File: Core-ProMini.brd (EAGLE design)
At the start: 99.8 x 68.8 mm, 27 parts, among them CON1 5.08, CON2 2mm, CON3 0.100, IC1 cj7805, J2 IO4, J4 2.1mm, J5 IO4, J6 IO4, J7 IO4

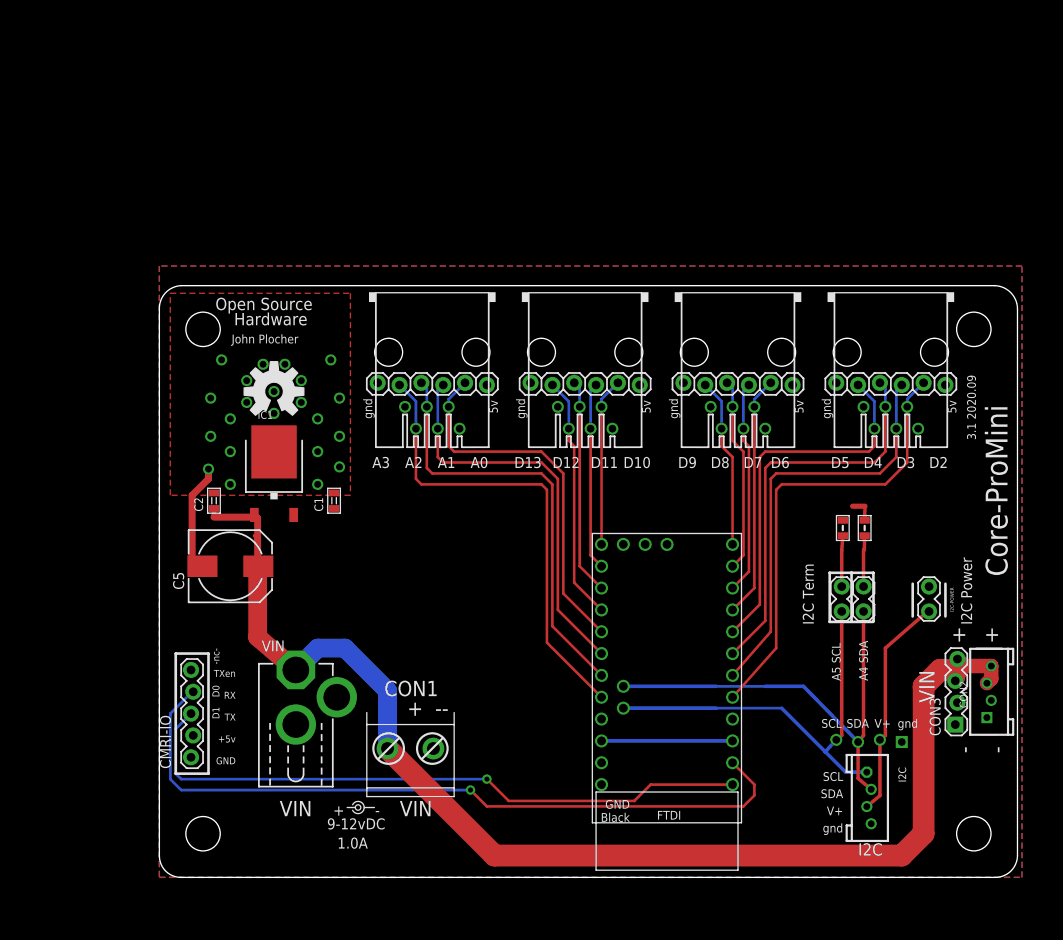
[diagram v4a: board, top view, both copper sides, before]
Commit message: normalized values
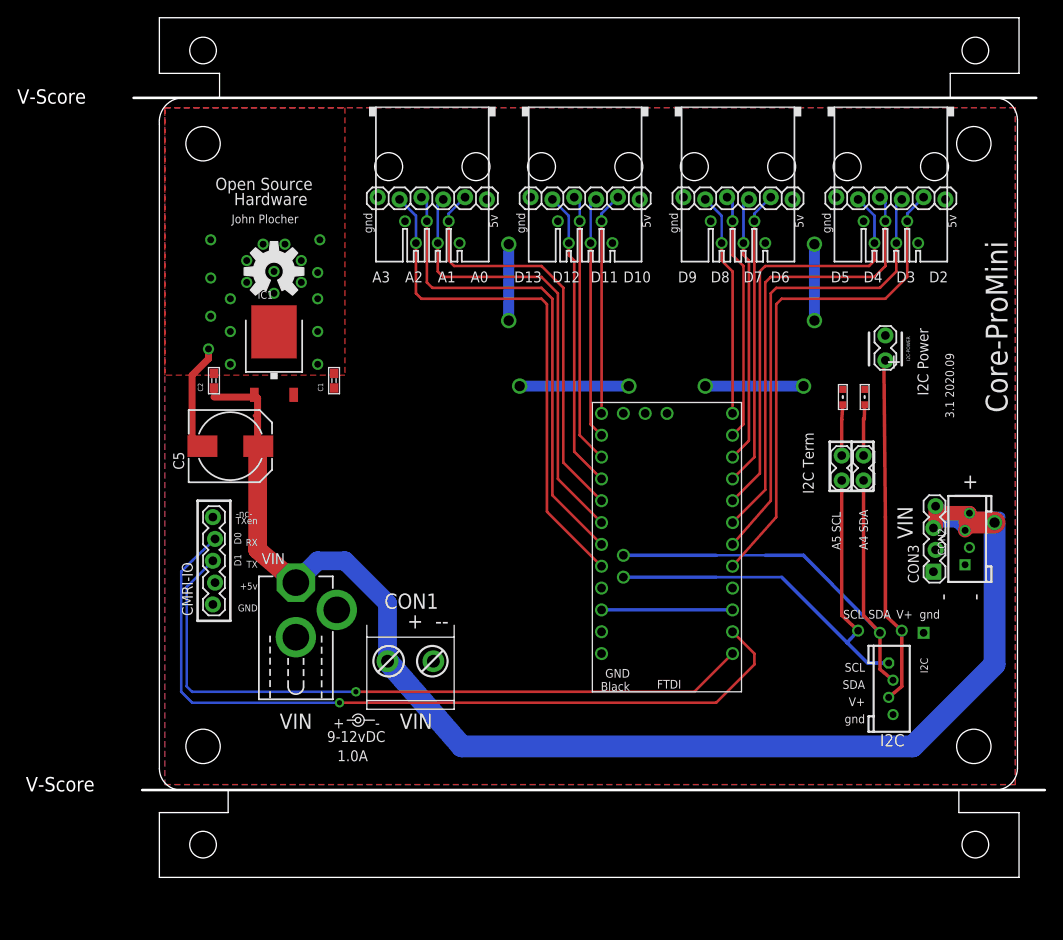
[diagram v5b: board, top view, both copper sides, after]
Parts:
- BOARD: value BOARD69X100MRCS -> BOARD; device SPCoast:BOARD-DINRAIL-2.71IN-MRCS -> SPCoast:BOARD-DINRAIL-3.17INX10CM
- C1, C2: device SPCoast:0805-CAP -> SPCoast:0603-CAP
- C5: value 150uF -> 220uF
- CON1: value 5.08 -> 0.200
- CPU: value ARDUINO-PRO-MINIDAVESROBOT -> DAVEK
- J2, J5, J6, J7: value IO4 -> RJ12/6
- OSH: value L -> OSHW
- R101, R111: device SPCoast:0805-RES -> SPCoast:0603-RES
- moved I2C-POWER 29.6 mm to (84.5, 60.3)
- moved J2 21.6 mm to (85.1, 82.7)
- moved J5 21.6 mm to (67.3, 82.7)
- moved J6 21.6 mm to (49.5, 82.7)
- moved J7 21.6 mm to (31.8, 82.7)
- moved JP10 21.6 mm to (91.4, 78.9)
- moved JP11 21.6 mm to (73.7, 78.9)
- moved JP12 21.6 mm to (55.9, 78.9)
- moved JP13 21.6 mm to (38.1, 78.9)
- moved CMRI-IO 18.0 mm to (6.35, 31.8)
- moved CON3 18.0 mm to (90.2, 35.6)
- moved CON2 18.0 mm to (94.0, 39.4)
- moved R101 15.2 mm to (82.0, 55.9)
- moved R111 15.2 mm to (79.5, 55.9)
- moved SCL 15.2 mm to (79.4, 48.9)
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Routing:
- net VCCIO: track 3.08 -> 41.9 mm, vias 0 -> 8
- net +9V: track 148.0 -> 180.4 mm, vias 0 -> 1
- net N$44: track 26.1 -> 40.9 mm
- net D0: track 86.0 -> 93.4 mm
- net D1: track 74.6 -> 81.5 mm
- net SDA: track 51.7 -> 58.3 mm
- net SCL: track 48.5 -> 55.2 mm
- net A3: track 54.2 -> 60.6 mm
- net D9: track 19.9 -> 26.2 mm
- net D7: track 24.9 -> 31.3 mm
- net D6: track 28.3 -> 34.6 mm
- net D5: track 43.4 -> 49.7 mm
- net D3: track 48.8 -> 55.2 mm
- net D13: track 28.5 -> 34.9 mm
- net D11: track 21.9 -> 28.2 mm
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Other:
- board size 99.8 x 68.8 mm -> 106 x 100 mm
